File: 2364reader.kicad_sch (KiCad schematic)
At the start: 2 parts, among them U1 2364, U2 27C64

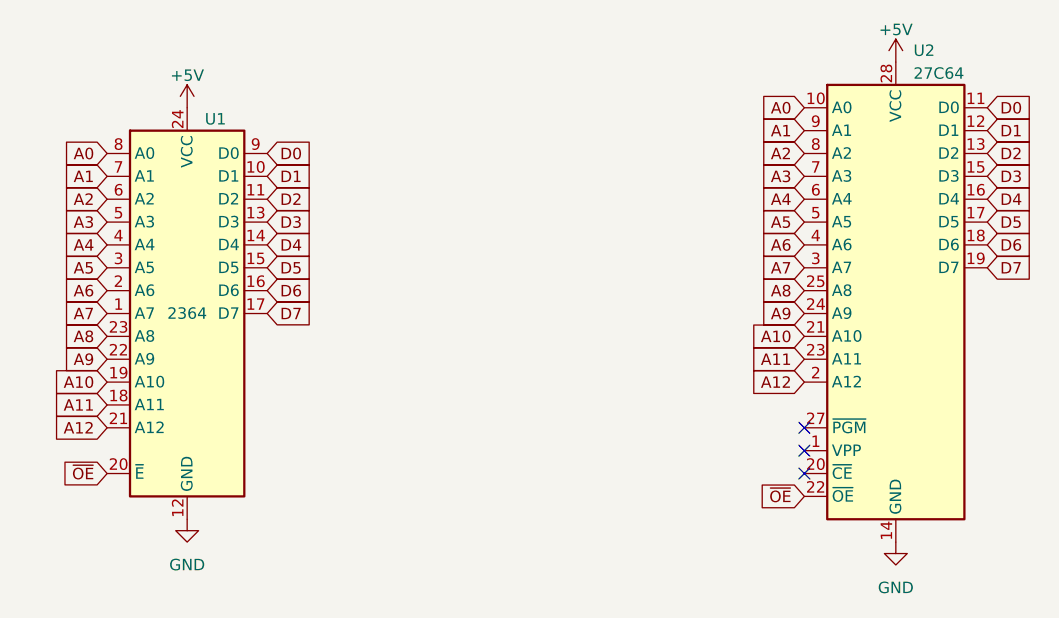
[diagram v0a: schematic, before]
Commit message: adapt to accept 2332
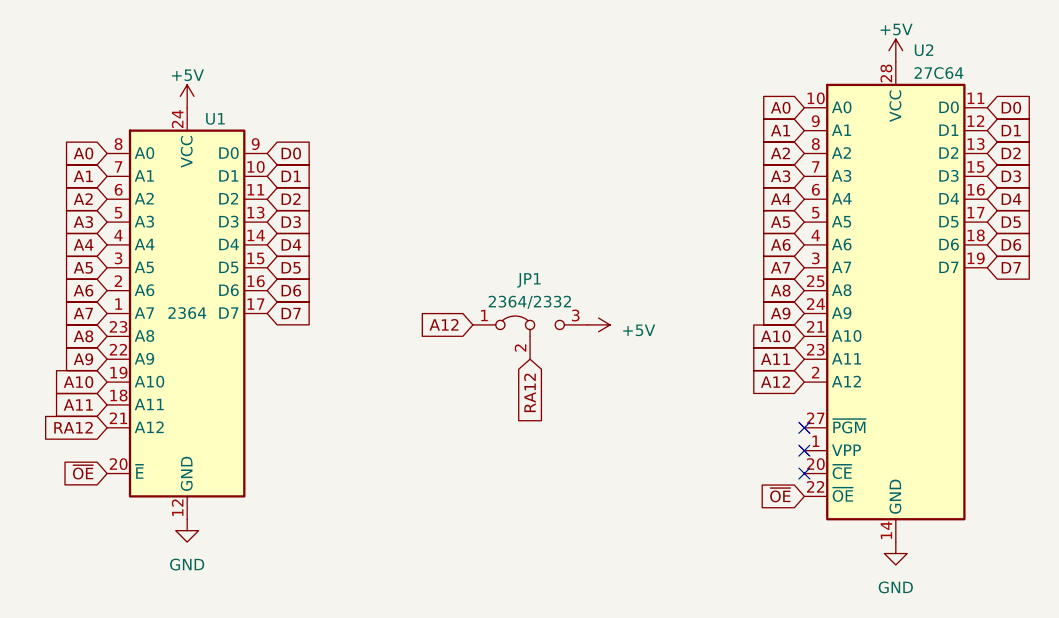
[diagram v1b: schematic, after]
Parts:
- added JP1: 2364/2332, Connector_PinHeader_2.54mm:PinHeader_1x03_P2.54mm_Horizontal, symbol Jumper:Jumper_3_Bridged12
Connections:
- net +5V: now also JP1.3 (B)
- net A12: now also JP1.1 (A); no longer U1.21 (A12)
- new net RA12: JP1.2 (C), U1.21 (A12)
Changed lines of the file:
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@@
     )
   )
-  (global_label "A12" (shape input) (at 86.36 107.95 180) (fields_autoplaced)
-    (effects (font (size 1.27 1.27)) (justify right))
-    (property "Intersheetrefs" "${INTERSHEET_REFS}" (at 81.1561 107.95 0)
+  (global_label "RA12" (shape input) (at 86.36 107.95 180) (fields_autoplaced)
+    (effects (font (size 1.27 1.27)) (justify right))
+    (property "Intersheetrefs" "${INTERSHEET_REFS}" (at 78.6766 107.95 0)
       (effects (font (size 1.27 1.27)) (justify right) hide)
     )
@@
     )
   )
+  (global_label "RA12" (shape input) (at 133.35 100.33 270) (fields_autoplaced)
+    (effects (font (size 1.27 1.27)) (justify right))
+    (property "Intersheetrefs" "${INTERSHEET_REFS}" (at 133.35 108.0134 90)
+      (effects (font (size 1.27 1.27)) (justify right) hide)
+    )
+  )
   (global_label "D1" (shape input) (at 184.15 74.93 0) (fields_autoplaced)
     (effects (font (size 1.27 1.27)) (justify left))
@@
     )
   )
+  (global_label "A12" (shape input) (at 127 96.52 180) (fields_autoplaced)
+    (effects (font (size 1.27 1.27)) (justify right))
+    (property "Intersheetrefs" "${INTERSHEET_REFS}" (at 121.7961 96.52 0)
+      (effects (font (size 1.27 1.27)) (justify right) hide)
+    )
+  )
   (global_label "A7" (shape input) (at 163.83 90.17 180) (fields_autoplaced)
     (effects (font (size 1.27 1.27)) (justify right))
@@
     (property "Intersheetrefs" "${INTERSHEET_REFS}" (at 81.1561 92.71 0)
       (effects (font (size 1.27 1.27)) (justify right) hide)
+    )
+  )
+  (symbol (lib_id "Jumper:Jumper_3_Bridged12") (at 133.35 96.52 0) (unit 1)
+    (in_bom yes) (on_board yes) (dnp no) (fields_autoplaced)
+    (property "Reference" "JP1" (at 133.35 91.44 0)
+      (effects (font (size 1.27 1.27)))
+    )
+    (property "Value" "2364/2332" (at 133.35 93.98 0)
+      (effects (font (size 1.27 1.27)))
+    )
+    (property "Footprint" "Connector_PinHeader_2.54mm:PinHeader_1x03_P2.54mm_Horizontal" (at 133.35 96.52 0)
+      (effects (font (size 1.27 1.27)) hide)
+    )
+    (property "Datasheet" "~" (at 133.35 96.52 0)
+      (effects (font (size 1.27 1.27)) hide)
+    )
+    (pin "1")
+    (pin "2")
+    (pin "3")
+    (instances
+      (project "2364reader"
+        (path "/ce74d7da-00b6-4f07-8114-218744816fcc"
+          (reference "JP1") (unit 1)
+        )
+      )
     )
   )
@@
         )
       )
+    )
+  )
+  (symbol (lib_id "power:+5V") (at 139.7 96.52 270) (unit 1)
+    (in_bom yes) (on_board yes) (dnp no) (fields_autoplaced)
+    (property "Reference" "#PWR05" (at 135.89 96.52 0)
+      (effects (font (size 1.27 1.27)) hide)
+    )
+    (property "Value" "+5V" (at 143.51 97.155 90)
+      (effects (font (size 1.27 1.27)) (justify left))
+    )
+    (property "Footprint" "" (at 139.7 96.52 0)
+      (effects (font (size 1.27 1.27)) hide)
+    )
+    (property "Datasheet" "" (at 139.7 96.52 0)
+      (effects (font (size 1.27 1.27)) hide)
+    )
+    (pin "1")
+    (instances
+      (project "2364reader"
+        (path "/ce74d7da-00b6-4f07-8114-218744816fcc"
+          (reference "#PWR05") (unit 1)
+        )
+      )

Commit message: revise board to fix 2332 problem
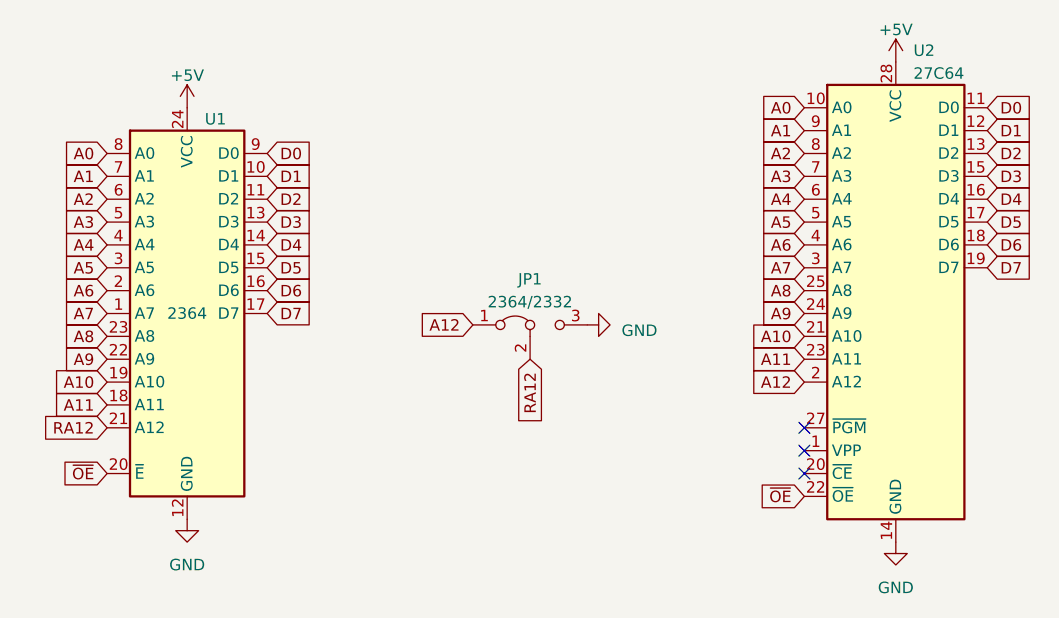
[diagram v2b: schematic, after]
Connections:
- net +5V: no longer JP1.3 (B)
- net GND: now also JP1.3 (B)
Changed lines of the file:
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@@
-    )
-  )
-  (symbol (lib_id "power:+5V") (at 139.7 96.52 270) (unit 1)
-    (in_bom yes) (on_board yes) (dnp no) (fields_autoplaced)
-    (property "Reference" "#PWR05" (at 135.89 96.52 0)
-      (effects (font (size 1.27 1.27)) hide)
-    )
-    (property "Value" "+5V" (at 143.51 97.155 90)
-      (effects (font (size 1.27 1.27)) (justify left))
-    )
-    (property "Footprint" "" (at 139.7 96.52 0)
-      (effects (font (size 1.27 1.27)) hide)
-    )
-    (property "Datasheet" "" (at 139.7 96.52 0)
-      (effects (font (size 1.27 1.27)) hide)
-    )
-    (pin "1")
-    (instances
-      (project "2364reader"
-        (path "/ce74d7da-00b6-4f07-8114-218744816fcc"
-          (reference "#PWR05") (unit 1)
-        )
-      )
     )
   )
@@
         )
       )
+    )
+  )
+  (symbol (lib_id "power:GND") (at 139.7 96.52 90) (unit 1)
+    (in_bom yes) (on_board yes) (dnp no) (fields_autoplaced)
+    (property "Reference" "#PWR05" (at 146.05 96.52 0)
+      (effects (font (size 1.27 1.27)) hide)
+    )
+    (property "Value" "GND" (at 143.51 97.155 90)
+      (effects (font (size 1.27 1.27)) (justify right))
+    )
+    (property "Footprint" "" (at 139.7 96.52 0)
+      (effects (font (size 1.27 1.27)) hide)
+    )
+    (property "Datasheet" "" (at 139.7 96.52 0)
+      (effects (font (size 1.27 1.27)) hide)
+    )
+    (pin "1")
+    (instances
+      (project "2364reader"
+        (path "/ce74d7da-00b6-4f07-8114-218744816fcc"
+          (reference "#PWR05") (unit 1)
+        )
+      )
